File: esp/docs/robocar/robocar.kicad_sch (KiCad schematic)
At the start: 5 parts, among them U4 ESP32-S3-DEVKITC-1-N16R8V

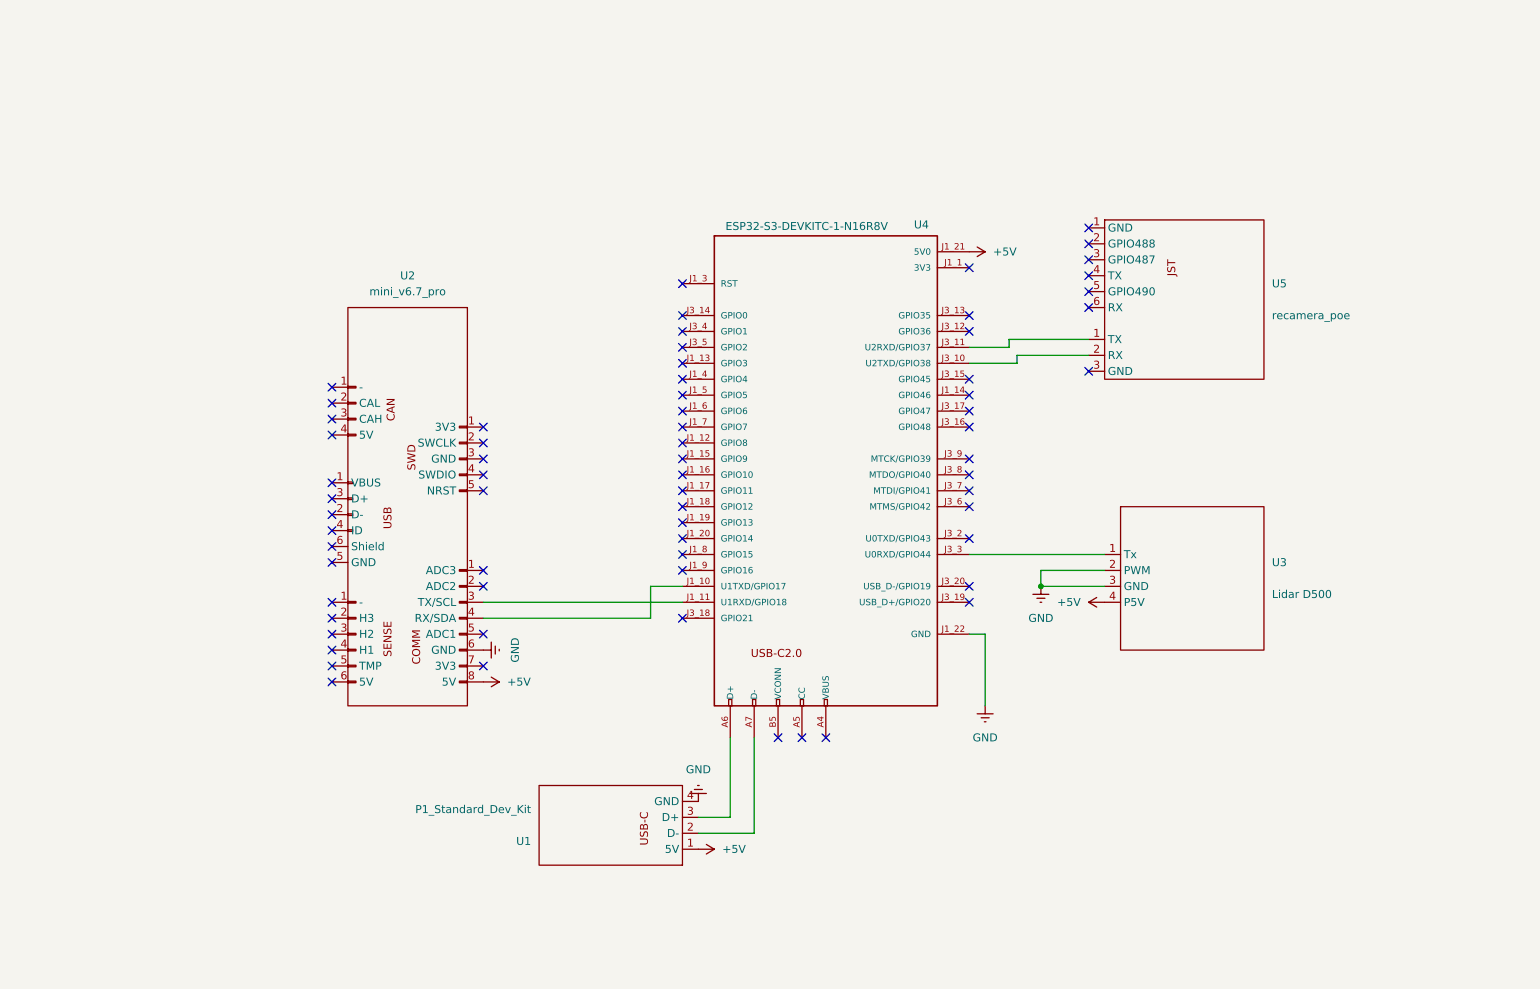
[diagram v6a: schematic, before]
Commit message: [UPD] Hardware schematic + gitignore
- gitignore ignores vscode files
- hardware schematic updated due to receival of an esp with a diff format
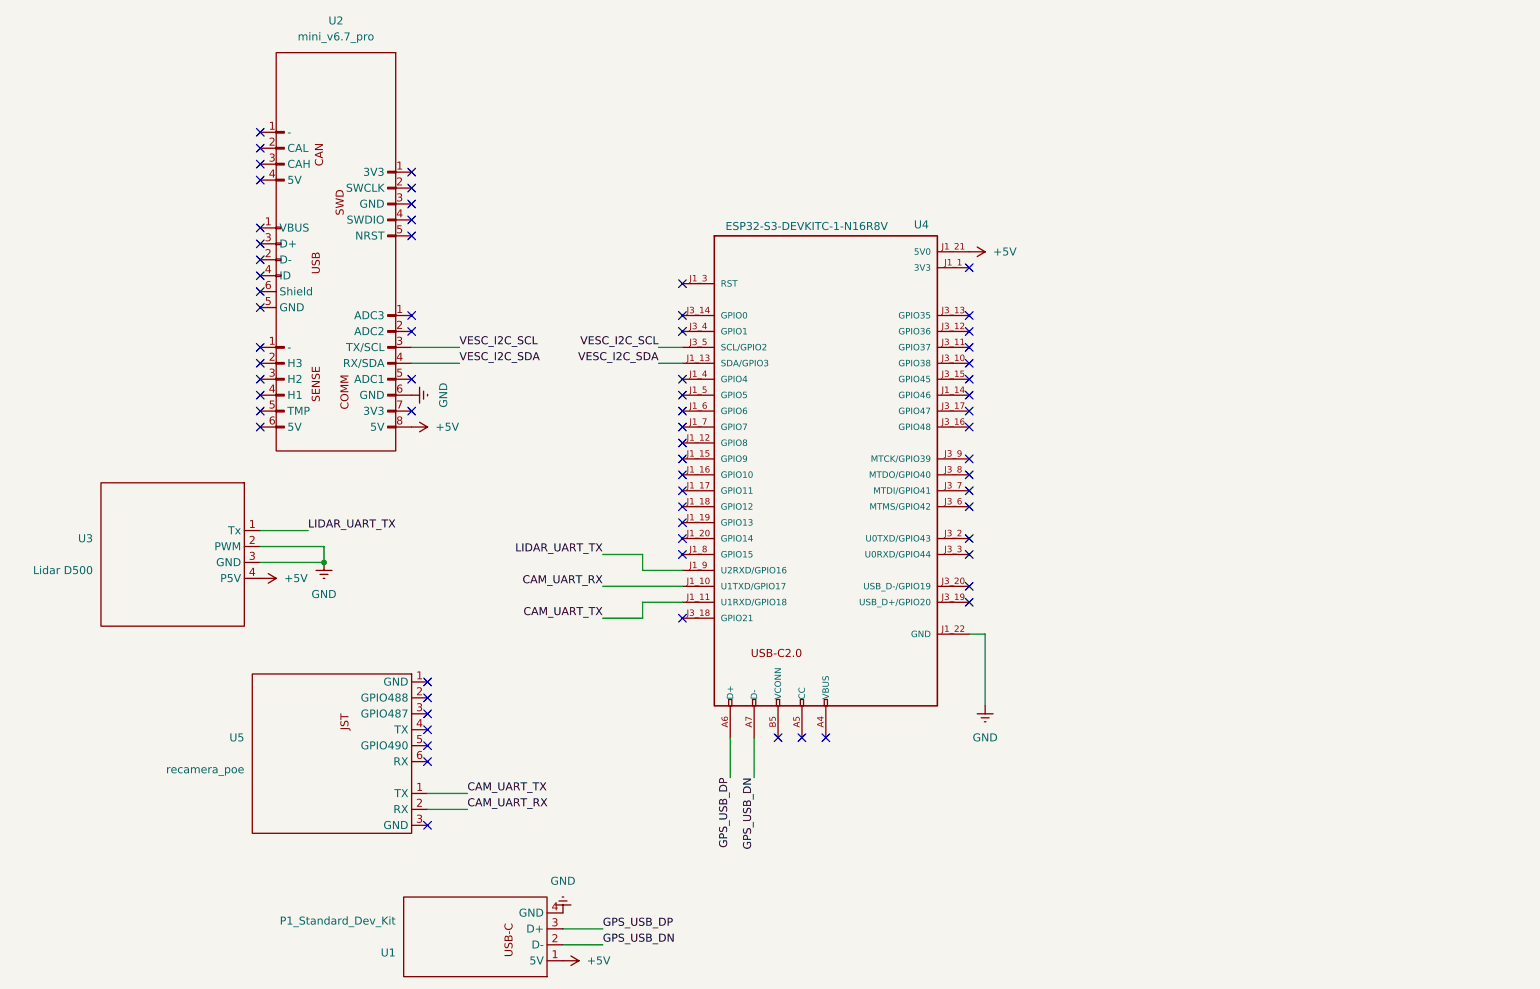
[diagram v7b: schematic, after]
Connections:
- net VESC_I2C_SCL: now reaches U2.3 (H2)
- net VESC_I2C_SCL: now also U4.J3_5 (SCL/GPIO2)
- net CAM_UART_TX: now reaches U4.J1_11 (U1RXD/GPIO18)
- net CAM_UART_TX: now also U5.1 (TX); no longer U2.3 (H2)
- net VESC_I2C_SDA: now reaches U2.4 (H1)
- net VESC_I2C_SDA: now also U4.J1_13 (SDA/GPIO3)
- net CAM_UART_RX: now reaches U4.J1_10 (U1TXD/GPIO17)
- net CAM_UART_RX: now also U5.2 (RX); no longer U2.4 (H1)
- net at U4.J3_11 (GPIO37): no longer U5.1 (TX)
- net at U4.J3_10 (GPIO38): no longer U5.2 (RX)
- net GPS_USB_DN: now reaches U1.2 (D-), U4.A7 (D-)
- net GPS_USB_DP: now reaches U1.3 (D+), U4.A6 (D+)
- net at U4.J3_3 (U0RXD/GPIO44): no longer U3.1 (Tx)
- net LIDAR_UART_TX: now reaches U4.J1_9 (U2RXD/GPIO16)
- net LIDAR_UART_TX: now also U3.1 (Tx)
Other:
- moved on the sheet: U1, U2, U3, U5

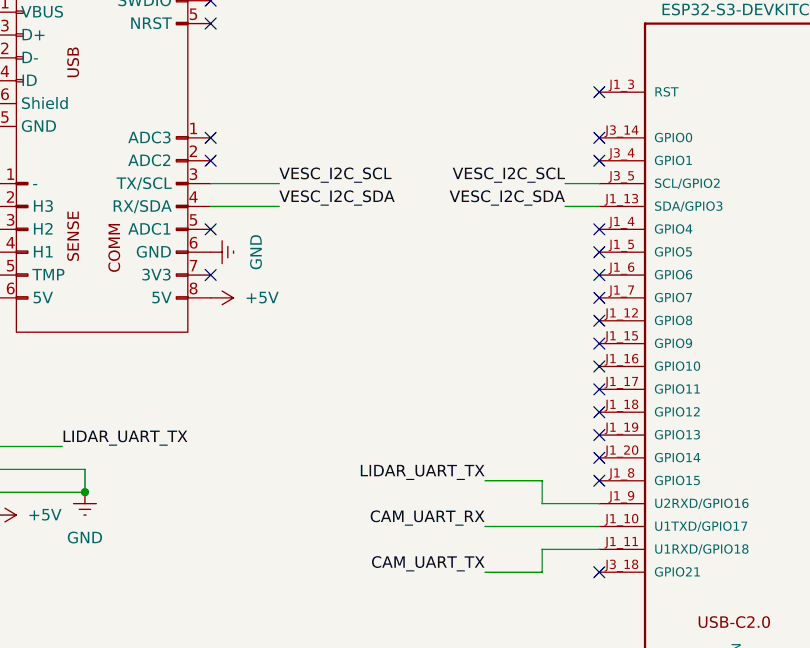
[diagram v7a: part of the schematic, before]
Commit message: [UPD] Hardware schematic
- Updated hardware schematic in order to adhere to the new split (lidar / vesc)
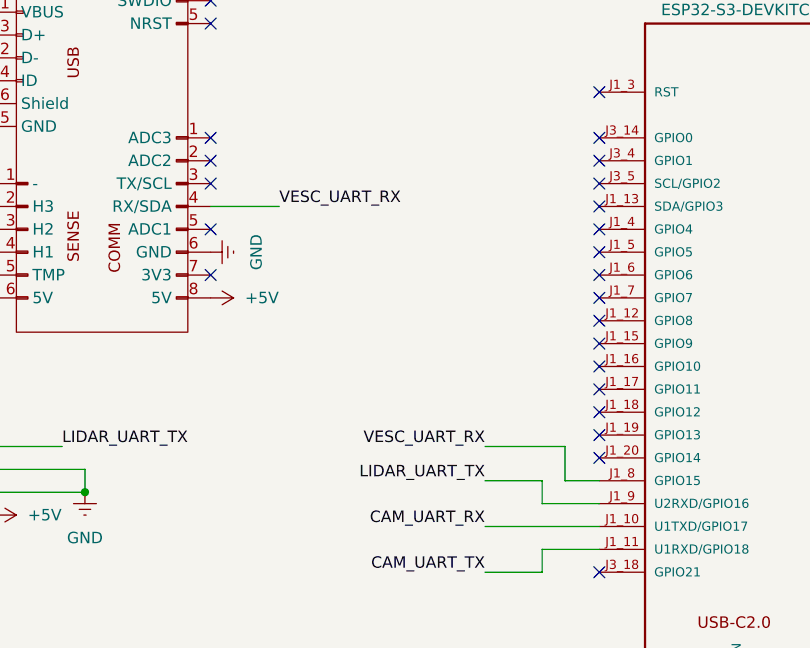
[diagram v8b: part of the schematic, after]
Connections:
- net VESC_UART_RX: now reaches U2.4 (H1)
- net VESC_UART_RX: now also U4.J1_8 (GPIO15)
- net VESC_I2C_SCL: no longer names the net of U4.J3_5 (SCL/GPIO2)
- net VESC_I2C_SCL: no longer U2.3 (H2)
- net VESC_I2C_SDA: no longer names the net of U4.J1_13 (SDA/GPIO3)
- net VESC_I2C_SDA: no longer U2.4 (H1)
- no-connect marks 68 -> 70
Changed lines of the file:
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@@
+	)
+	(no_connect
+		(at 127 74.93)
 	)
 	(no_connect
@@
 	)
 	(no_connect
+		(at 127 77.47)
+	)
+	(no_connect
 		(at 83.82 57.15)
 	)
@@
 	)
 	(no_connect
+		(at 83.82 74.93)
+	)
+	(no_connect
 		(at 127 82.55)
 	)
@@
 	)
 	(no_connect
-		(at 127 107.95)
-	)
-	(no_connect
 		(at 83.82 49.53)
 	)
@@
 	(wire
 		(pts
-			(xy 123.19 77.47) (xy 127 77.47)
-		)
-		(stroke
-			(width 0)
-			(type default)
-		)
-	)
-	(wire
-		(pts
-			(xy 123.19 74.93) (xy 127 74.93)
-		)
-		(stroke
-			(width 0)
-			(type default)
-			(color 255 153 0 1)
+			(xy 123.19 107.95) (xy 123.19 104.14)
+		)
+		(stroke
+			(width 0)
+			(type default)
+			(color 0 132 132 1)
 		)
 	)
@@
 	(wire
 		(pts
+			(xy 127 107.95) (xy 123.19 107.95)
+		)
+		(stroke
+			(width 0)
+			(type default)
+			(color 0 132 132 1)
+		)
+	)
+	(wire
+		(pts
 			(xy 114.3 118.11) (xy 120.65 118.11)
 		)
@@
 			(width 0)
 			(type default)
-			(color 0 132 0 1)
+			(color 0 194 194 1)
 		)
 	)
@@
 	(wire
 		(pts
+			(xy 114.3 104.14) (xy 123.19 104.14)
+		)
+		(stroke
+			(width 0)
+			(type default)
+			(color 0 132 132 1)
+		)
+	)
+	(wire
+		(pts
 			(xy 114.3 113.03) (xy 127 113.03)
 		)
@@
 	(wire
 		(pts
-			(xy 83.82 74.93) (xy 91.44 74.93)
-		)
-		(stroke
-			(width 0)
-			(type default)
-			(color 255 153 0 1)
-		)
-	)
-	(wire
-		(pts
 			(xy 92.71 148.59) (xy 86.36 148.59)
 		)
@@
 		)
 	)
-	(label "VESC_I2C_SCL"
-		(at 91.44 74.93 0)
-		(effects
-			(font
-				(size 1.27 1.27)
-			)
-			(justify left bottom)
-		)
-	)
-	(label "VESC_I2C_SDA"
+	(label "VESC_UART_RX"
 		(at 91.44 77.47 0)
 		(effects
@@
 		)
 	)
-	(label "VESC_I2C_SDA"
-		(at 123.19 77.47 180)
-		(effects
-			(font
-				(size 1.27 1.27)
-			)
-			(justify right bottom)
-		)
-	)
 	(label "LIDAR_UART_TX"
 		(at 67.31 104.14 0)
@@
 		)
 	)
+	(label "VESC_UART_RX"
+		(at 114.3 104.14 180)
+		(effects
+			(font
+				(size 1.27 1.27)
+			)
+			(justify right bottom)
+		)
+	)
 	(label "GPS_USB_DP"
 		(at 114.3 167.64 0)
@@
 		)
 	)
-	(label "VESC_I2C_SCL"
-		(at 123.19 74.93 180)
-		(effects
-			(font
-				(size 1.27 1.27)
-			)
-			(justify right bottom)
-		)
-	)
